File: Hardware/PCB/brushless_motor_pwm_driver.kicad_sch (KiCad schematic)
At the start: 4 parts, among them U7 DS3232M

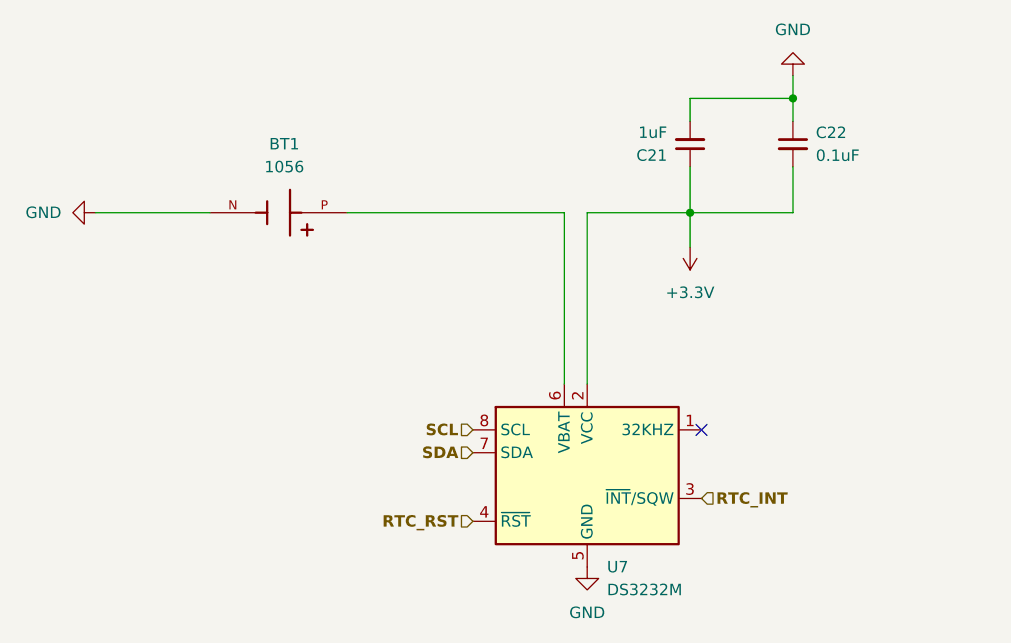
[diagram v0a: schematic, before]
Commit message: overall design is pretty much done, starting layout and routing now
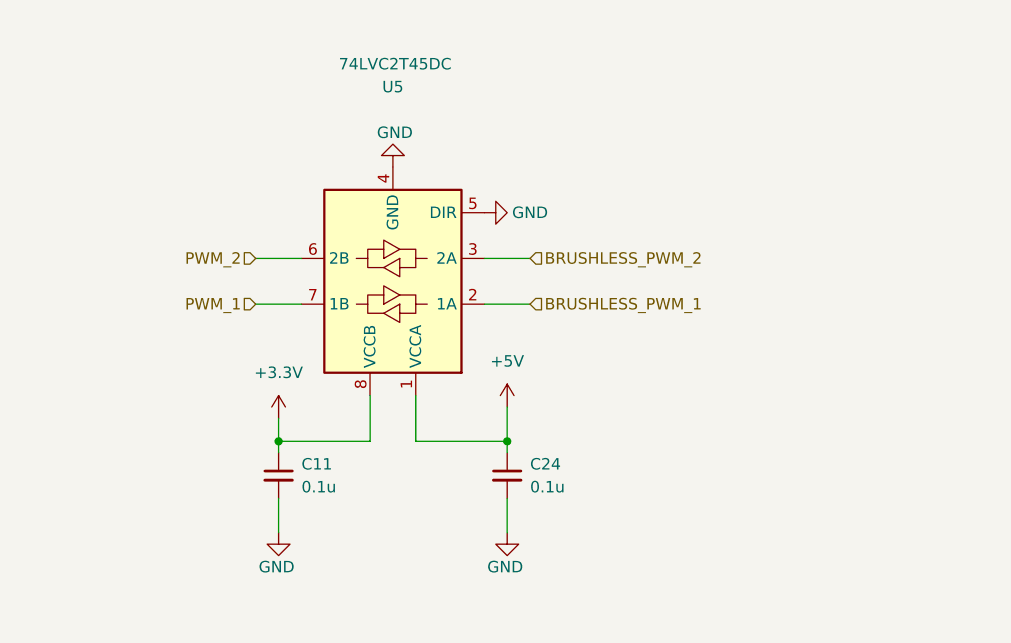
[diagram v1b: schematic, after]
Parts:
- removed BT1: 1056, Vendor_Footprints:BAT_1056, symbol Vendor_Symbols:1056
- removed C21: 1uF, Capacitor_SMD:C_0603_1608Metric_Pad1.08x0.95mm_HandSolder, symbol Device:C_Small
- removed C22: 0.1uF, Capacitor_SMD:C_0603_1608Metric_Pad1.08x0.95mm_HandSolder, symbol Device:C_Small
- removed U7: DS3232M, Package_SO:SOIC-8_3.9x4.9mm_P1.27mm, symbol Timer_RTC:DS3232M
- added C11, C24: 0.1u, Capacitor_SMD:C_0603_1608Metric_Pad1.08x0.95mm_HandSolder, symbol Device:C_Small
- added U5: 74LVC2T45DC, Package_SO:VSSOP-8_2.3x2mm_P0.5mm, symbol Logic_LevelTranslator:74LVCH2T45DC
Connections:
- net +3.3V: now also C11.1, U5.8 (VCCB)
- net GND: now also C11.2, C24.2, U5.4 (GND), U5.5 (DIR)
- new net +5V: C24.1, U5.1 (VCCA)
- new net BRUSHLESS_PWM_1: U5.2 (1A)
- new net BRUSHLESS_PWM_2: U5.3 (2A)
- new net PWM_1: U5.7 (1B)
- new net PWM_2: U5.6 (2B)
- no-connect marks 1 -> 0

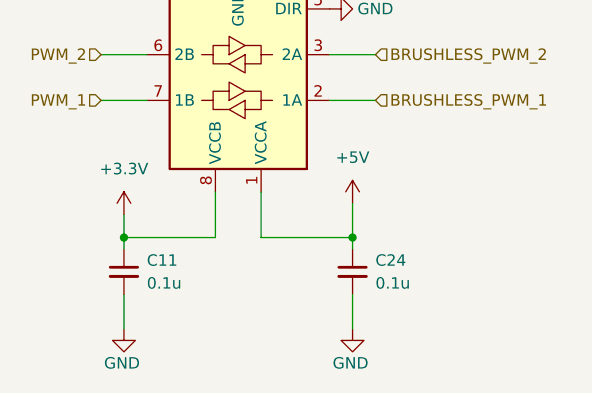
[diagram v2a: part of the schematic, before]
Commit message: fixed BOM, added some silkscreen, getting quote now
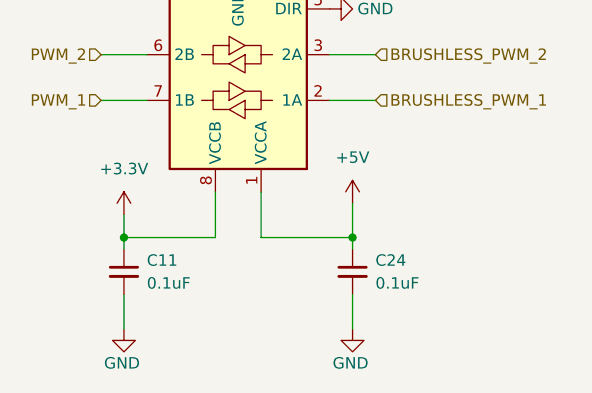
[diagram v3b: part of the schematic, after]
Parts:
- C11, C24: value 0.1u -> 0.1uF
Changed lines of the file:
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@@
 			)
 		)
-		(property "Value" "0.1u"
+		(property "Value" "0.1uF"
 			(at 90.17 74.9362 0)
 			(effects
@@
 			)
 		)
-		(property "Value" "0.1u"
+		(property "Value" "0.1uF"
 			(at 115.57 74.9362 0)
 			(effects

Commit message: kinda pricey, I should try to make a smaller version using LCSC parts for cheaper solution
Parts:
- C11, C24: LCSC (none) -> C66501
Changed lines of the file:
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@@
+			)
+		)
+		(property "LCSC" "C66501"
+			(at 87.63 73.66 0)
+			(effects
+				(font
+					(size 1.27 1.27)
+				)
 			)
 		)
@@
 			)
 		)
+		(property "LCSC" ""
+			(at 100.33 52.07 0)
+			(effects
+				(font
+					(size 1.27 1.27)
+				)
+			)
+		)
 		(pin "4"
 		)
@@
 			)
 		)
+		(property "LCSC" "C66501"
+			(at 113.03 73.66 0)
+			(effects
+				(font
+					(size 1.27 1.27)
+				)
+			)
+		)

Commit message: done with this, placed order
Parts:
- removed U5: 74LVC2T45DC, Package_SO:VSSOP-8_2.3x2mm_P0.5mm, symbol Logic_LevelTranslator:74LVCH2T45DC
- added J3, J4: BLDC Motor, Vendor_Footprints:CONN_WJ15EDGRC-3.81-3P, symbol Connector:Screw_Terminal_01x03
- added U2: SN74LVC2T45DCUR, Package_SO:VSSOP-8_2.3x2mm_P0.5mm, symbol Logic_LevelTranslator:SN74LVC2T45DCUR
- C11, C24: value 0.1uF -> 100nF; LCSC C66501 -> C14663; MPN CL10B104KO8NNNC -> CC0603KRX7R9BB104; Manufacturer Samsung Electro-Mechanics -> YAGEO
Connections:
- net +3.3V: now also U2.8 (VCCB)
- net +5V: now also U2.1 (VCCA)
- net GND: now also J3.3 (Pin_3), J4.3 (Pin_3), U2.4 (GND), U2.5 (DIR)
- new net: J3.2 (Pin_2), U2.2 (A1)
- new net: J4.2 (Pin_2), U2.3 (A2)
- new net +24V: J3.1 (Pin_1), J4.1 (Pin_1)
- new net Pump_PWM: U2.6 (B2)
- new net Vac_PWM: U2.7 (B1)
